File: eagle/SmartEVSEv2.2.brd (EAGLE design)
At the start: 86 x 50 mm, 73 parts, among them CON1 3.5MM_12PIN, CON3 JST_10PIN_FFC, IC1 AOZ1280CI, IC2 LM7332MA, IC3 MCP9700A, IC4 PIC18F26K22-I/SOSSOP, IC5 SN65HVD72, IC6 FAN3214TMX, IC7 TC7660S, K1 AQH1213AX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

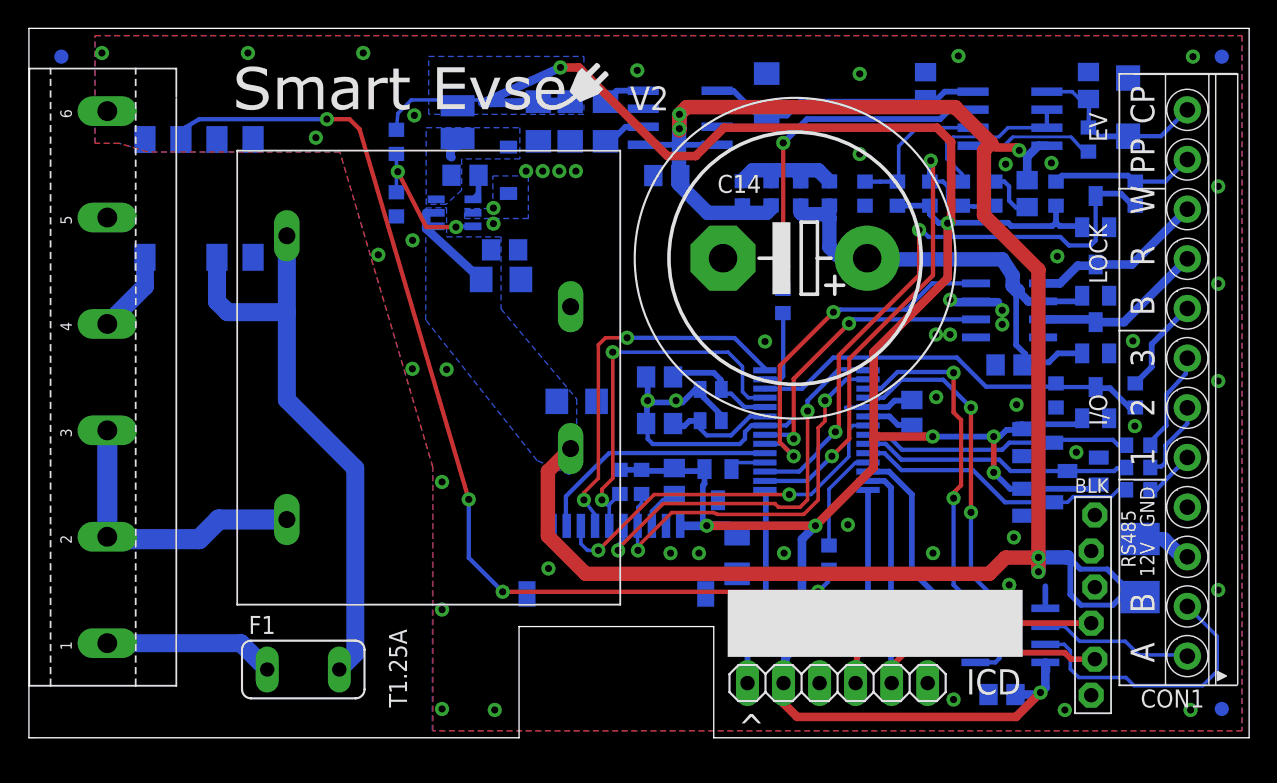
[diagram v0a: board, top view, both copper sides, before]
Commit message: Updated Schematics
Updated schematic and board to version 2.2
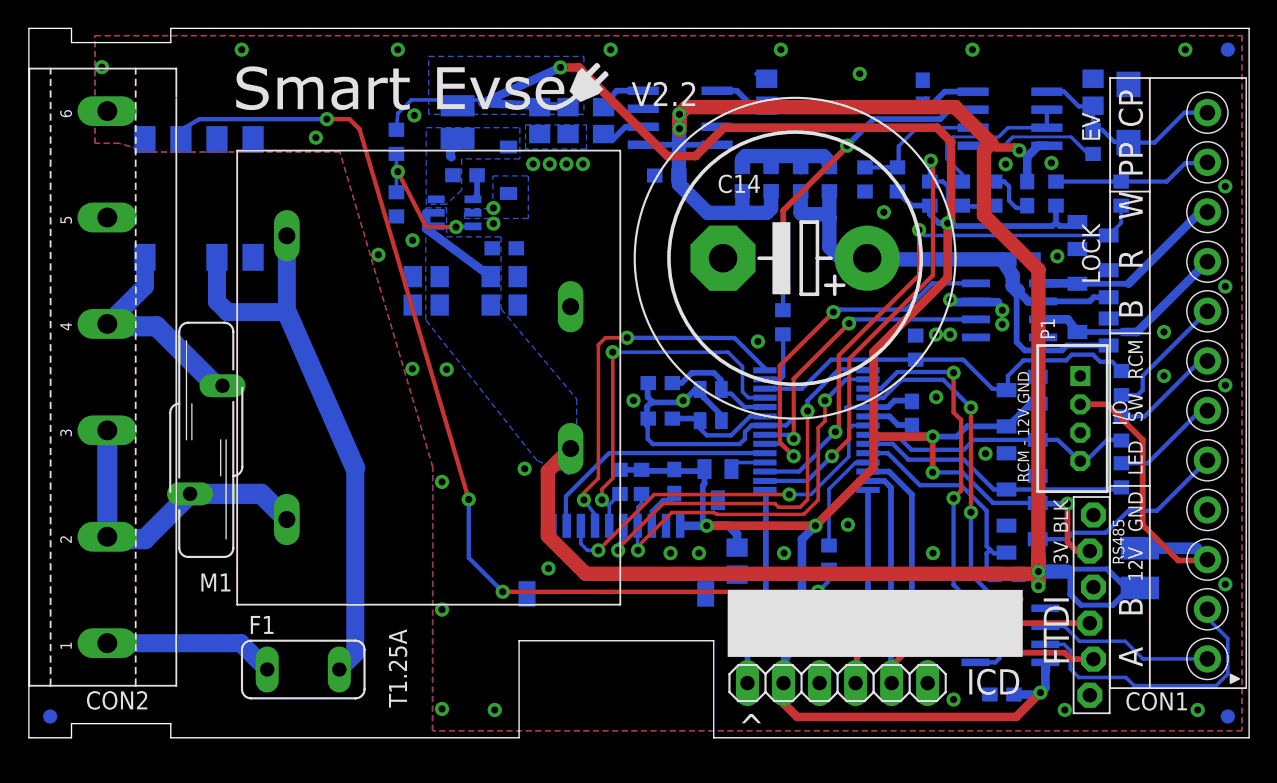
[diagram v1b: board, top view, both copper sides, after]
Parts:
- removed D7: BAT54S, diode:SOT23
- added C20, C22: 10u16v, rcl:C0805
- added M1: V275LA20AP, varistor:S14K40
- added P1: B4B-PH-K, con-jst-ph:B4B-PH-K
- added T1: BSS138, adafruit:SOT23
- C1, C10, C11, C13, C17, C19, C2, C21, C4, C5, C8: device rcl:C0805 -> rcl:C0603
- C12, C15, C16, C18, C3, C9: device rcl:C1206 -> rcl:C0805
- C7: value np -> 10u16v; device rcl:C1206 -> rcl:C0805
- CON2: value AST027-06 -> DG128-7.5
- F2: value 0.1A MC36205 -> 0.2A Polyfuse; device adafruit:1812 -> adafruit:R1210
- R13: value 100R -> 10K
- moved U$1 46.5 mm to (1.50, 1.50)
- moved C16 13.8 mm to (28.0, 32.5), turned to 0 degrees
- moved R13 11.0 mm to (68.9, 11.5), turned to 0 degrees
- moved R16 10.4 mm to (62.5, 27.5), turned to 270 degrees
- moved C13 7.49 mm to (69.9, 33.7), turned to 180 degrees
- moved D3 5.26 mm to (70.0, 24.5), turned to 270 degrees
- moved D8 4.49 mm to (70.0, 17.5)
- moved CON1 4.40 mm to (82.5, 24.5)
- moved D2 1.69 mm to (75.0, 35.4), turned to 90 degrees
- moved R18 1.67 mm to (77.0, 21.8), turned to 90 degrees
- moved R2 1.50 mm to (53.1, 29.3)
- moved R1 1.31 mm to (77.0, 25.0), turned to 270 degrees
- moved R15 1.31 mm to (77.0, 18.5), turned to 90 degrees
- moved D9 1.12 mm to (70.0, 21.0)
- moved R11 1.00 mm to (77.0, 38.4)
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- renumbered X2 to CON2
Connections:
- removed net N$31: CON1.3, F2.1
- removed net N$4: CON1.5, R13.2
- new net 12V_FUSED: CON1.3, F2.1, P1.2
- new net LED_12V: CON1.5, T1.3
- net +12V: now also C20.1, C22.1
- net GND: now also C20.2, C22.2, P1.1, R13.1, T1.2; no longer D7.1
- net IO1: now also R13.2, T1.1; no longer D7.3, R13.1
- net IO3: now also P1.4
- net N$23: now also M1.2
- net N$26: now also M1.1
- net VCC: now also FTDI.5; no longer D7.2
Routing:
- net 12V_FUSED: track 0.00 -> 22.1 mm
- net LED_12V: track 0.00 -> 14.3 mm
- net N$23: track 5.80 -> 15.7 mm
- net VCC: track 192.9 -> 198.4 mm
- net N$17: track 35.6 -> 40.6 mm
- net N$31: track 3.86 -> 0.00 mm
- net IO1: track 20.0 -> 16.3 mm
- net N$4: track 3.59 -> 0.00 mm
- net N$16: track 42.3 -> 39.2 mm
- net +12V: track 149.8 -> 152.6 mm
- net N$33: track 6.80 -> 9.09 mm
- net N$10: track 13.1 -> 15.1 mm
- net N$27: track 12.1 -> 14.1 mm
- net N$34: track 5.71 -> 7.60 mm
- net N$11: track 5.85 -> 4.35 mm
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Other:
- outline, holes or cut-outs redrawn
- board text added: "3V"
- board text added: "CON2"
- board text added: "FTDI"
- board text added: "LED"
- board text added: "RCM"
- board text added: "RCM - 12V GND"
- board text added: "SW"
- board text added: "V2.2"
- board text removed: "1"
- board text removed: "2"
- board text removed: "3"
- board text removed: "RS485"
- board text removed: "V2"
